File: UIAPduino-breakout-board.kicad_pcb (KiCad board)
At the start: 2 copper layers, 56.6 x 54.1 mm, 14 parts, among them J1 Conn_01x20_Pin, J2 Conn_01x20_Socket, J3 Barrel_Jack_Switch, SW1 SW_SPDT_312, SW2 SW_SPDT_312, SW3 SW_Slide_DPDT, U3 L7805

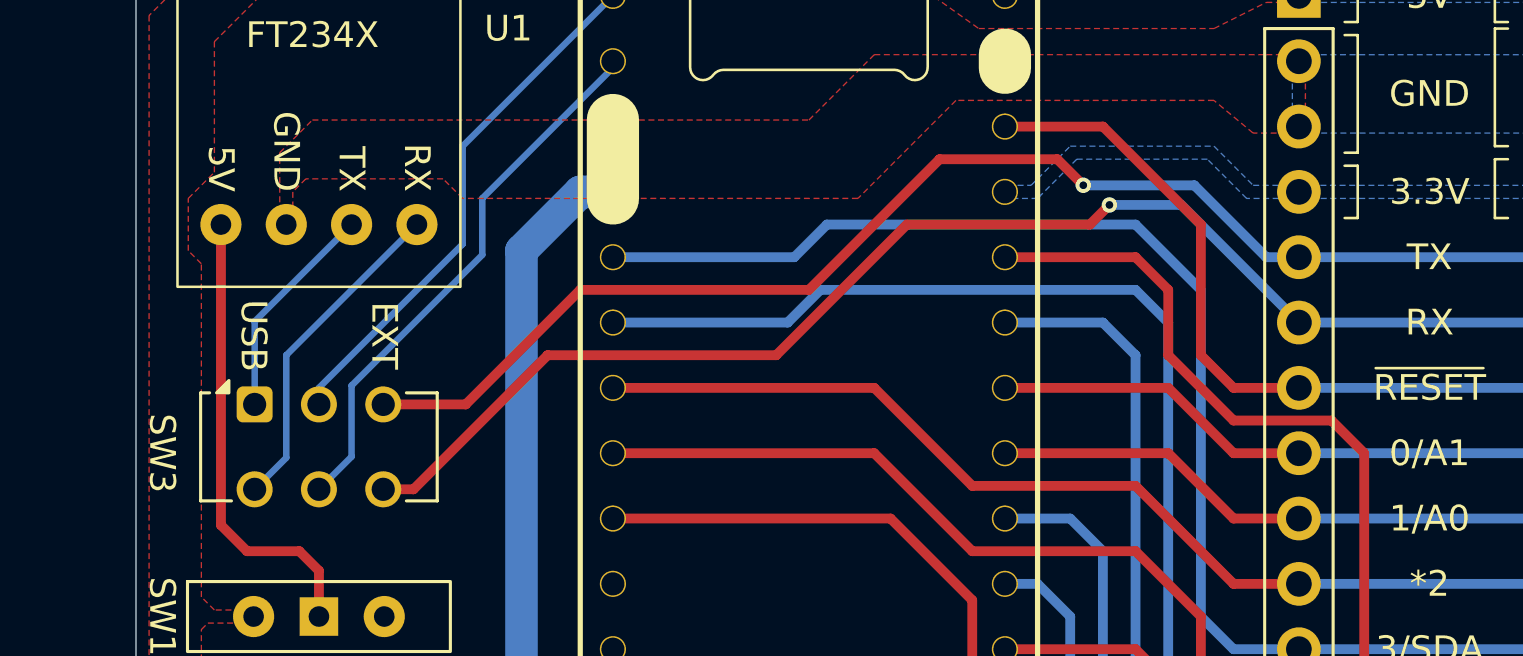
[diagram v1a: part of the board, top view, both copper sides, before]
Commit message: 配線を見直して via を除去
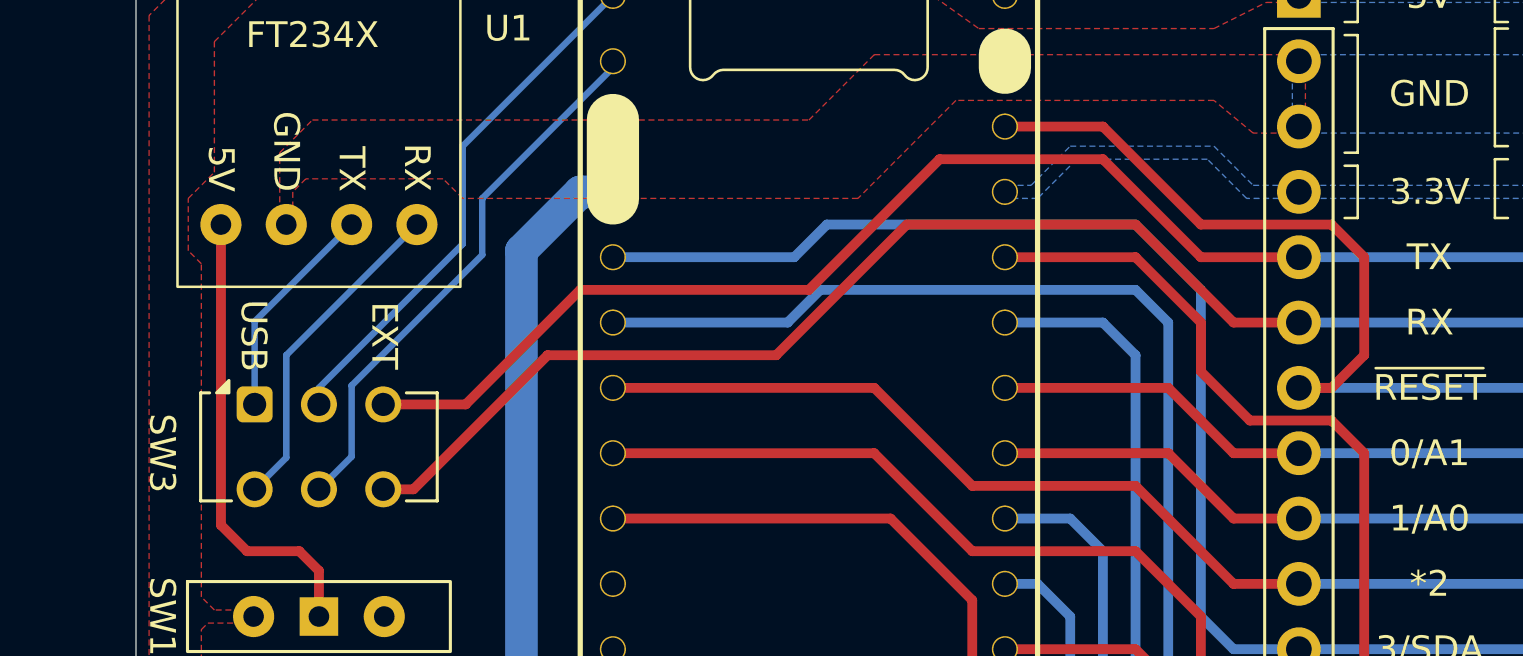
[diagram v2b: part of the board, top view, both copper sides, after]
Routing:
- net Net-(J1-Pin_7): track 28.8 -> 33.1 mm
- net /EXT_RX: track 52.2 -> 51.6 mm, vias 1 -> 0
- net /EXT_TX: track 51.4 -> 51.3 mm, vias 1 -> 0
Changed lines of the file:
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@@
 		(tags "switch DPDT")
 		(property "Reference" "SW3"
-			(at -3.596 1.8965 270)
+			(at -3.596 1.8965 -90)
 			(unlocked yes)
 			(layer "F.SilkS")
@@
 	)
 	(segment
-		(start 166.37 78.74)
-		(end 166.37 81.28)
+		(start 173.99 114.3)
+		(end 172.72 115.57)
 		(width 0.381)
 		(layer "F.Cu")
@@
 	)
 	(segment
-		(start 165.1 77.47)
-		(end 166.37 78.74)
+		(start 172.72 83.82)
+		(end 173.99 85.09)
 		(width 0.381)
 		(layer "F.Cu")
@@
 	)
 	(segment
-		(start 173.99 114.3)
-		(end 172.72 115.57)
+		(start 173.99 85.09)
+		(end 173.99 114.3)
 		(width 0.381)
 		(layer "F.Cu")
@@
 	)
 	(segment
-		(start 172.72 83.82)
-		(end 173.99 85.09)
+		(start 172.72 115.57)
+		(end 171.45 115.57)
 		(width 0.381)
 		(layer "F.Cu")
@@
 	)
 	(segment
-		(start 166.37 81.28)
-		(end 168.91 83.82)
+		(start 167.64 81.915)
+		(end 169.545 83.82)
 		(width 0.381)
 		(layer "F.Cu")
@@
 	)
 	(segment
-		(start 172.72 115.57)
-		(end 171.45 115.57)
+		(start 160.02 77.47)
+		(end 165.1 77.47)
 		(width 0.381)
 		(layer "F.Cu")
@@
 	)
 	(segment
-		(start 168.91 83.82)
+		(start 169.545 83.82)
 		(end 172.72 83.82)
 		(width 0.381)
@@
 	)
 	(segment
-		(start 160.02 77.47)
-		(end 165.1 77.47)
+		(start 165.1 77.47)
+		(end 167.64 80.01)
 		(width 0.381)
 		(layer "F.Cu")
@@
 	)
 	(segment
-		(start 173.99 85.09)
-		(end 173.99 114.3)
+		(start 167.64 80.01)
+		(end 167.64 81.915)
 		(width 0.381)
 		(layer "F.Cu")
@@
 	)
 	(segment
-		(start 171.45 82.55)
-		(end 168.91 82.55)
+		(start 167.64 76.2)
+		(end 172.72 76.2)
+		(width 0.381)
+		(layer "F.Cu")
+		(net 18)
+	)
+	(segment
+		(start 172.72 76.2)
+		(end 173.99 77.47)
+		(width 0.381)
+		(layer "F.Cu")
+		(net 18)
+	)
+	(segment
+		(start 173.99 81.28)
+		(end 172.72 82.55)
 		(width 0.381)
 		(layer "F.Cu")
@@
 	)
 	(segment
-		(start 167.64 81.28)
-		(end 167.64 76.2)
+		(start 173.99 77.47)
+		(end 173.99 81.28)
 		(width 0.381)
 		(layer "F.Cu")
@@
 	)
 	(segment
-		(start 168.91 82.55)
-		(end 167.64 81.28)
+		(start 172.72 82.55)
+		(end 171.45 82.55)
 		(width 0.381)
 		(layer "F.Cu")
@@
 	)
 	(segment
-		(start 163.068 74.672786)
-		(end 162.055214 73.66)
+		(start 143.51 78.74)
+		(end 139.0565 83.1935)
 		(width 0.381)
 		(layer "F.Cu")
@@
 	)
 	(segment
-		(start 143.51 78.74)
-		(end 139.0565 83.1935)
+		(start 167.64 77.47)
+		(end 163.83 73.66)
 		(width 0.381)
 		(layer "F.Cu")
@@
 	)
 	(segment
-		(start 162.055214 73.66)
-		(end 157.48 73.66)
-		(width 0.381)
-		(layer "F.Cu")
-		(net 25)
-	)
-	(segment
 		(start 152.4 78.74)
 		(end 143.51 78.74)
@@
 		(net 25)
 	)
-	(via
-		(at 163.068 74.672786)
-		(size 0.6)
-		(drill 0.3)
-		(layers "F.Cu" "B.Cu")
-		(net 25)
-	)
-	(segment
-		(start 163.068 74.672786)
-		(end 163.071214 74.676)
-		(width 0.381)
-		(layer "B.Cu")
-		(net 25)
-	)
-	(segment
-		(start 167.386 74.676)
-		(end 170.18 77.47)
-		(width 0.381)
-		(layer "B.Cu")
-		(net 25)
-	)
-	(segment
-		(start 170.18 77.47)
-		(end 171.45 77.47)
-		(width 0.381)
-		(layer "B.Cu")
-		(net 25)
-	)
 	(segment
-		(start 163.068 74.672786)
-		(end 162.956786 74.672786)
+		(start 171.45 77.47)
+		(end 167.64 77.47)
 		(width 0.381)
-		(layer "B.Cu")
+		(layer "F.Cu")
 		(net 25)
 	)
 	(segment
-		(start 163.071214 74.676)
-		(end 167.386 74.676)
+		(start 163.83 73.66)
+		(end 157.48 73.66)
 		(width 0.381)
-		(layer "B.Cu")
+		(layer "F.Cu")
 		(net 25)
 	)
@@
 	)
 	(segment
-		(start 137.0265 86.4935)
-		(end 135.85 86.4935)
+		(start 168.91 80.01)
+		(end 171.45 80.01)
 		(width 0.381)
 		(layer "F.Cu")
@@
 	)
 	(segment
-		(start 163.322 76.2)
-		(end 156.21 76.2)
+		(start 165.1 76.2)
+		(end 168.91 80.01)
 		(width 0.381)
 		(layer "F.Cu")
@@
 	)
 	(segment
-		(start 151.13 81.28)
-		(end 142.24 81.28)
-		(width 0.381)
-		(layer "F.Cu")
-		(net 26)
-	)
-	(segment
-		(start 142.24 81.28)
+		(start 135.85 86.4935)
 		(end 137.0265 86.4935)
 		(width 0.381)
@@
 	)
 	(segment
-		(start 164.084 75.438)
-		(end 163.322 76.2)
+		(start 151.13 81.28)
+		(end 156.21 76.2)
 		(width 0.381)
 		(layer "F.Cu")
@@
 	)
 	(segment
-		(start 156.21 76.2)
+		(start 142.24 81.28)
 		(end 151.13 81.28)
 		(width 0.381)
@@
 		(net 26)
 	)
-	(via
-		(at 164.084 75.438)
-		(size 0.6)
-		(drill 0.3)
-		(layers "F.Cu" "B.Cu")
-		(net 26)
-	)
 	(segment
-		(start 171.45 80.01)
-		(end 181.61 80.01)
+		(start 137.0265 86.4935)
+		(end 142.24 81.28)
 		(width 0.381)
-		(layer "B.Cu")
+		(layer "F.Cu")
 		(net 26)
 	)
 	(segment
-		(start 166.878 75.438)
-		(end 164.084 75.438)
+		(start 156.21 76.2)
+		(end 165.1 76.2)
 		(width 0.381)
-		(layer "B.Cu")
+		(layer "F.Cu")
 		(net 26)
 	)
 	(segment
 		(start 171.45 80.01)
-		(end 166.878 75.438)
+		(end 181.61 80.01)
 		(width 0.381)
 		(layer "B.Cu")

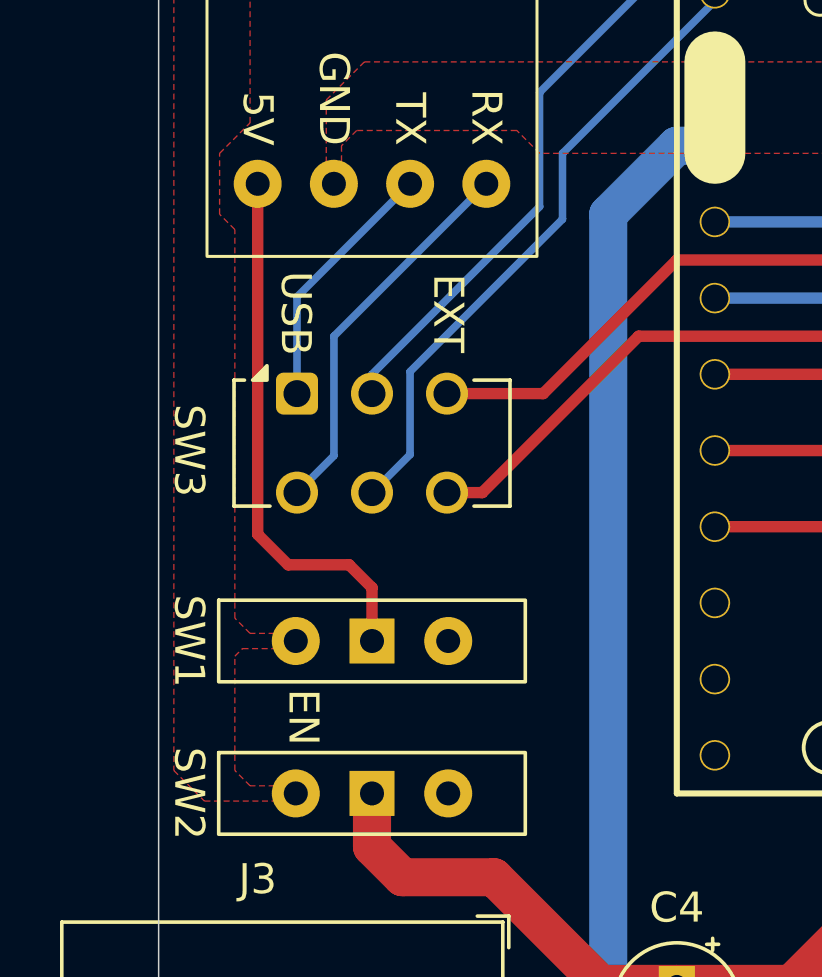
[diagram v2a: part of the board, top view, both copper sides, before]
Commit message: 配線修正
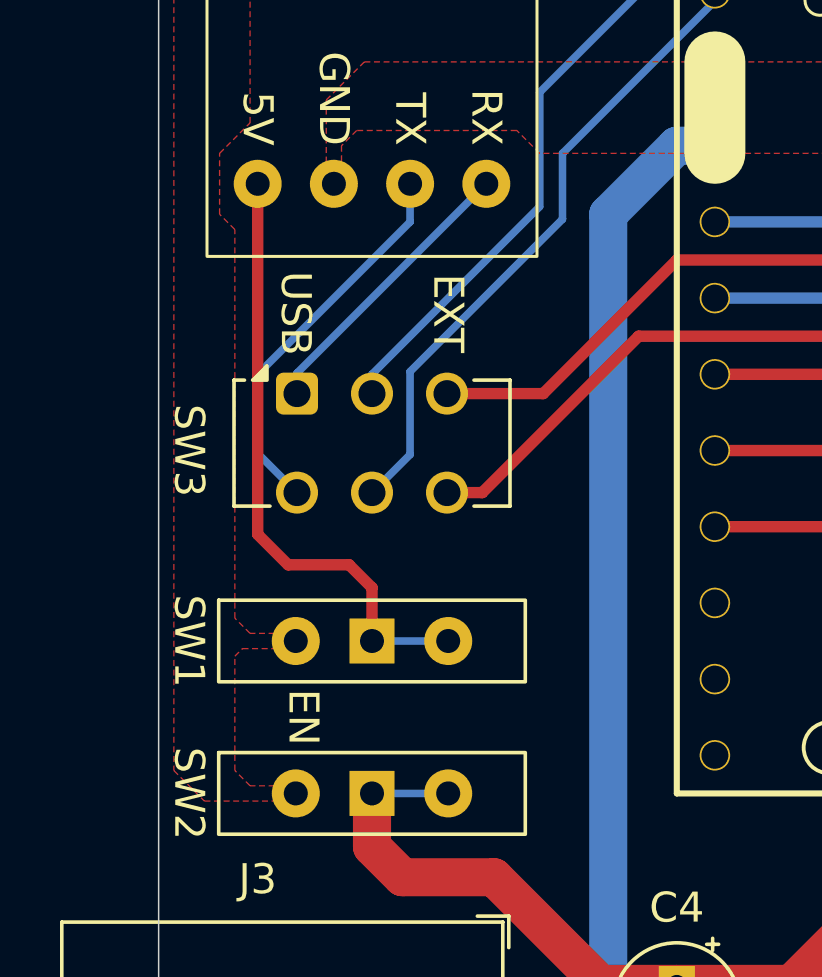
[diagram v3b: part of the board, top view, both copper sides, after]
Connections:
- SW1 pad 1: Net-(SW1-B) -> Net-(SW1-A)
- SW1 pad 3: unconnected-(SW1-A-Pad3) -> Net-(SW1-A)
- SW2 pad 3: unconnected-(SW2-A-Pad3) -> Net-(D1-A)
- SW3 pad 1: /USB_TX -> /USB_RX
- SW3 pad 6: /USB_RX -> /USB_TX
- U1 pad 1: Net-(SW1-B) -> Net-(SW1-A)
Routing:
- net Net-(SW1-A): track 0.00 -> 20.5 mm
- net Net-(SW1-B): track 18.0 -> 0.00 mm
- net /USB_TX: track 8.56 -> 12.9 mm
- net /USB_RX: track 12.9 -> 9.61 mm
- net Net-(D1-A): track 38.1 -> 40.6 mm
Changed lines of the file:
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@@
 	(net 15 "Net-(J1-Pin_12)")
 	(net 16 "Net-(J1-Pin_14)")
-	(net 17 "Net-(SW1-B)")
+	(net 17 "Net-(SW1-A)")
 	(net 18 "Net-(J1-Pin_7)")
 	(net 19 "+12V")
 	(net 20 "Net-(D1-A)")
-	(net 21 "unconnected-(SW1-A-Pad3)")
-	(net 22 "unconnected-(SW2-A-Pad3)")
-	(net 23 "/UIAP_TX")
-	(net 24 "/UIAP_RX")
-	(net 25 "/EXT_TX")
-	(net 26 "/EXT_RX")
-	(net 27 "/USB_TX")
-	(net 28 "/USB_RX")
+	(net 21 "/UIAP_TX")
+	(net 22 "/UIAP_RX")
+	(net 23 "/EXT_TX")
+	(net 24 "/EXT_RX")
+	(net 25 "/USB_TX")
+	(net 26 "/USB_RX")
 	(footprint "akizuki:FT234X"
 		(layer "F.Cu")
@@
 			(layers "*.Cu" "*.Mask")
 			(remove_unused_layers no)
-			(net 17 "Net-(SW1-B)")
+			(net 17 "Net-(SW1-A)")
 			(pinfunction "5V")
 			(pintype "power_out")
@@
 			(layers "*.Cu" "*.Mask")
 			(remove_unused_layers no)
-			(net 27 "/USB_TX")
+			(net 25 "/USB_TX")
 			(pinfunction "TX")
 			(pintype "output")
@@
 			(layers "*.Cu" "*.Mask")
 			(remove_unused_layers no)
-			(net 28 "/USB_RX")
+			(net 26 "/USB_RX")
 			(pinfunction "RX")
 			(pintype "input")
@@
 			(remove_unused_layers no)
 			(roundrect_rratio 0.1785714286)
-			(net 27 "/USB_TX")
+			(net 26 "/USB_RX")
 			(pinfunction "A")
 			(pintype "passive")
@@
 			(layers "*.Cu" "*.Mask")
 			(remove_unused_layers no)
-			(net 23 "/UIAP_TX")
+			(net 21 "/UIAP_TX")
 			(pinfunction "B")
 			(pintype "passive")
@@
 			(layers "*.Cu" "*.Mask")
 			(remove_unused_layers no)
-			(net 25 "/EXT_TX")
+			(net 23 "/EXT_TX")
 			(pinfunction "C")
 			(pintype "passive")
@@
 			(layers "*.Cu" "*.Mask")
 			(remove_unused_layers no)
-			(net 26 "/EXT_RX")
+			(net 24 "/EXT_RX")
 			(pinfunction "A")
 			(pintype "passive")
@@
 			(layers "*.Cu" "*.Mask")
 			(remove_unused_layers no)
-			(net 24 "/UIAP_RX")
+			(net 22 "/UIAP_RX")
 			(pinfunction "B")
 			(pintype "passive")
@@
 			(layers "*.Cu" "*.Mask")
 			(remove_unused_layers no)
-			(net 28 "/USB_RX")
+			(net 25 "/USB_TX")
 			(pinfunction "C")
 			(pintype "passive")
@@
 			(layers "*.Cu" "*.Mask")
 			(remove_unused_layers no)
-			(net 17 "Net-(SW1-B)")
+			(net 17 "Net-(SW1-A)")
 			(pinfunction "B")
 			(pintype "passive")
@@
 			(layers "*.Cu" "*.Mask")
 			(remove_unused_layers no)
-			(net 21 "unconnected-(SW1-A-Pad3)")
+			(net 17 "Net-(SW1-A)")
 			(pinfunction "A")
-			(pintype "passive+no_connect")
+			(pintype "passive")
 		)
 		(model "${KICAD8_3DMODEL_DIR}/Button_Switch_THT.3dshapes/SW_Slide-03_Wuerth-WS-SLTV_10x2.5x6.4_P2.54mm.wrl"
@@
 			(layers "*.Cu" "*.Mask")
 			(remove_unused_layers no)
-			(net 22 "unconnected-(SW2-A-Pad3)")
+			(net 20 "Net-(D1-A)")
 			(pinfunction "A")
-			(pintype "passive+no_connect")
+			(pintype "passive")
 		)
 		(model "${KICAD8_3DMODEL_DIR}/Button_Switch_THT.3dshapes/SW_Slide-03_Wuerth-WS-SLTV_10x2.5x6.4_P2.54mm.wrl"
@@
 			(layers "*.Cu" "*.Mask")
 			(remove_unused_layers no)
-			(net 25 "/EXT_TX")
+			(net 23 "/EXT_TX")
 			(pinfunction "Pin_5")
 			(pintype "passive")
@@
 			(layers "*.Cu" "*.Mask")
 			(remove_unused_layers no)
-			(net 26 "/EXT_RX")
+			(net 24 "/EXT_RX")
 			(pinfunction "Pin_6")
 			(pintype "passive")
@@
 			(layers "*.Cu" "*.Paste" "*.Mask")
 			(remove_unused_layers no)
-			(net 23 "/UIAP_TX")
+			(net 21 "/UIAP_TX")
 			(pinfunction "15/A5(TX)")
 			(pintype "bidirectional")
@@
 			(layers "*.Cu" "*.Paste" "*.Mask")
 			(remove_unused_layers no)
-			(net 24 "/UIAP_RX")
+			(net 22 "/UIAP_RX")
 			(pinfunction "16/A6(RX)")
 			(pintype "bidirectional")
@@
 			(layers "*.Cu" "*.Mask")
 			(remove_unused_layers no)
-			(net 25 "/EXT_TX")
+			(net 23 "/EXT_TX")
 			(pinfunction "Pin_5")
 			(pintype "passive")
@@
 			(layers "*.Cu" "*.Mask")
 			(remove_unused_layers no)
-			(net 26 "/EXT_RX")
+			(net 24 "/EXT_RX")
 			(pinfunction "Pin_6")
 			(pintype "passive")
@@
 	)
 	(segment
+		(start 135.89 91.44)
+		(end 133.35 91.44)
+		(width 0.254)
+		(layer "B.Cu")
+		(net 17)
+	)
+	(segment
 		(start 167.64 76.2)
 		(end 172.72 76.2)
@@
 	)
 	(segment
+		(start 135.89 96.52)
+		(end 133.35 96.52)
+		(width 0.254)
+		(layer "B.Cu")
+		(net 20)
+	)
+	(segment
 		(start 138.938 73.152)
 		(end 138.938 76.962)
 		(width 0.254)
 		(layer "B.Cu")
-		(net 23)
+		(net 21)
 	)
 	(segment
@@
 		(width 0.254)
 		(layer "B.Cu")
-		(net 23)
+		(net 21)
 	)
 	(segment
@@
 		(width 0.254)
 		(layer "B.Cu")
-		(net 23)
+		(net 21)
 	)
 	(segment
@@
 		(width 0.254)
 		(layer "B.Cu")
-		(net 23)
+		(net 21)
 	)
 	(segment
@@
 		(width 0.254)
 		(layer "B.Cu")
-		(net 24)
+		(net 22)
 	)
 	(segment
@@
 		(width 0.254)
 		(layer "B.Cu")
-		(net 24)
+		(net 22)
 	)
 	(segment
@@
 		(width 0.254)
 		(layer "B.Cu")
-		(net 24)
+		(net 22)
 	)
 	(segment
@@
 		(width 0.254)
 		(layer "B.Cu")
-		(net 24)
+		(net 22)
 	)
 	(segment
@@
 		(width 0.254)
 		(layer "B.Cu")
-		(net 24)
+		(net 22)
 	)
 	(segment
@@
 		(width 0.254)
 		(layer "B.Cu")
-		(net 24)
+		(net 22)
 	)
 	(segment
@@
 		(width 0.381)
 		(layer "F.Cu")
-		(net 25)
+		(net 23)
 	)
 	(segment
@@
 		(width 0.381)
 		(layer "F.Cu")
-		(net 25)
+		(net 23)
 	)
 	(segment
@@
 		(width 0.381)
 		(layer "F.Cu")
-		(net 25)
+		(net 23)
 	)
 	(segment
@@
 		(width 0.381)
 		(layer "F.Cu")
-		(net 25)
+		(net 23)
 	)
 	(segment
@@
 		(width 0.381)
 		(layer "F.Cu")
-		(net 25)
+		(net 23)
 	)
 	(segment
@@
 		(width 0.381)
 		(layer "F.Cu")
-		(net 25)
+		(net 23)
 	)
 	(segment
@@
 		(width 0.381)
 		(layer "F.Cu")
-		(net 25)
+		(net 23)
 	)
 	(segment
@@
 		(width 0.381)
 		(layer "B.Cu")
-		(net 25)
+		(net 23)
 	)
 	(segment
@@
 		(width 0.381)
 		(layer "F.Cu")
-		(net 26)
+		(net 24)
 	)
 	(segment
@@
 		(width 0.381)
 		(layer "F.Cu")
-		(net 26)
+		(net 24)
 	)
 	(segment
@@
 		(width 0.381)
 		(layer "F.Cu")
-		(net 26)
+		(net 24)
 	)
 	(segment
@@
 		(width 0.381)
 		(layer "F.Cu")
-		(net 26)
+		(net 24)
 	)
 	(segment
@@
 		(width 0.381)
 		(layer "F.Cu")
-		(net 26)
+		(net 24)
 	)
 	(segment
@@
 		(width 0.381)
 		(layer "F.Cu")
-		(net 26)
+		(net 24)
 	)
 	(segment
@@
 		(width 0.381)
 		(layer "F.Cu")
-		(net 26)
+		(net 24)
 	)
 	(segment
@@
 		(width 0.381)
 		(layer "B.Cu")
-		(net 26)
+		(net 24)
 	)
 	(segment
 		(start 134.62 76.2)
-		(end 130.85 79.97)
+		(end 134.62 77.47)
 		(width 0.254)
 		(layer "B.Cu")
-		(net 27)
+		(net 25)
 	)
 	(segment
-		(start 130.85 79.97)
-		(end 130.85 83.1935)
+		(start 134.62 77.47)
+		(end 129.54 82.55)
 		(width 0.254)
 		(layer "B.Cu")
-		(net 27)
+		(net 25)
 	)
 	(segment
-		(start 137.16 76.2)
-		(end 132.08 81.28)
+		(start 129.54 85.1835)
+		(end 130.85 86.4935)
 		(width 0.254)
 		(layer "B.Cu")
-		(net 28)
+		(net 25)
 	)
 	(segment
-		(start 132.08 85.2635)
-		(end 130.85 86.4935)
+		(start 129.54 82.55)
+		(end 129.54 85.1835)
+		(width 0.254)
+		(layer "B.Cu")
+		(net 25)
+	)
+	(segment
+		(start 130.85 83.1935)
+		(end 130.85 82.51)
 		(width 0.254)
 		(layer "B.Cu")
-		(net 28)
+		(net 26)
 	)
 	(segment
-		(start 132.08 81.28)
-		(end 132.08 85.2635)
+		(start 130.85 82.51)
+		(end 137.16 76.2)
 		(width 0.254)
 		(layer "B.Cu")
-		(net 28)
+		(net 26)
 	)
 	(zone
